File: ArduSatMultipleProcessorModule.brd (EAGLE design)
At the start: 95.5 x 90.3 mm, 86 parts, among them IC1 ATMEGA328P, IC2 ATMEGA328P, IC3 ATMEGA328P, IC4 ATMEGA328P, IC7 ATMEGA328P, IC8 MCP23S17ML, P1 N1_ICSP, P2 N0_ICSP, P3 N0_ICSP, P4 N1_ICSP, P5 N1_ICSP, Q1 BSS138 N-MOSFET, Q10 2N7002 N-MOSFET, Q11 BSS138 N-MOSFET, Q12 BSS138 N-MOSFET, Q2 BSS138 N-MOSFET, Q3 BSS138 N-MOSFET, Q4 BSS138 N-MOSFET, Q5 BSS138 N-MOSFET, Q6 BSS138 N-MOSFET, Q7 BSS138 N-MOSFET, Q8 BSS138 N-MOSFET, Q9 2N7002 N-MOSFET

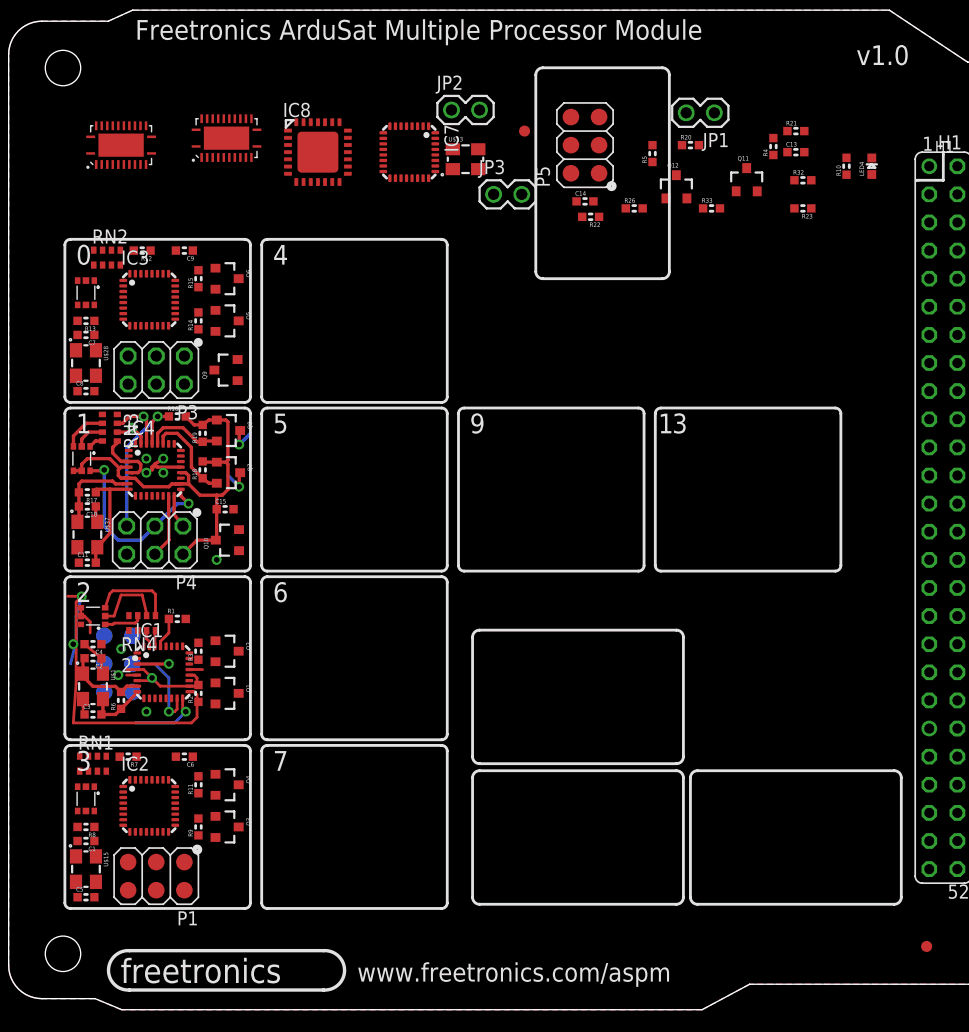
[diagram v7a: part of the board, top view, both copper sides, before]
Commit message: Added parts for remaining nodes
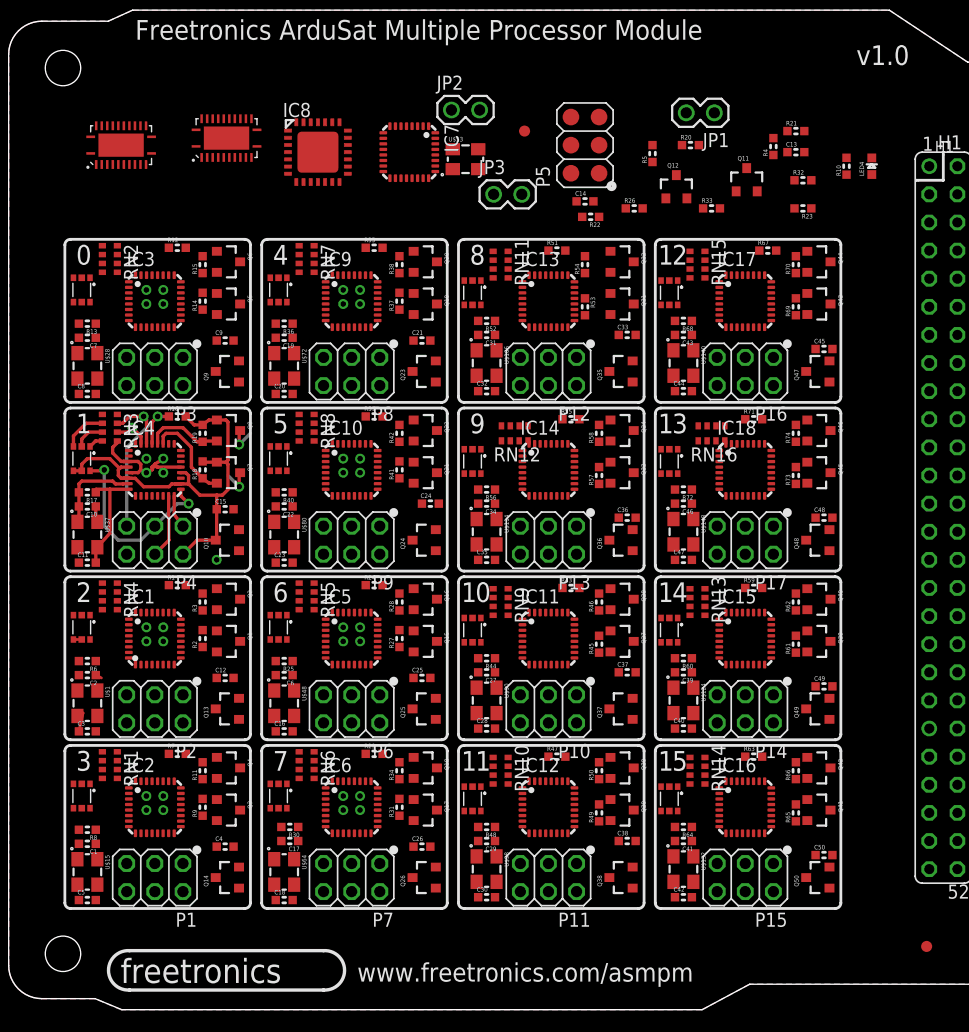
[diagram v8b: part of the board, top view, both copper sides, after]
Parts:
- added C12, C21, C24, C25, C26, C33, C36, C37, C38, C45, C48, C49, C50: 100nF 0603, freetronics-master-v1.1:0603
- added C16, C17, C18, C19, C20, C22, C23, C27, C28, C29, C30, C31, C32, C34, C35, C39, C40, C41, C42, C43, C44, C46, C47: 22pF 0603, freetronics-master-v1.1:0603
- added IC10, IC11, IC12, IC13, IC14, IC15, IC16, IC17, IC18, IC5, IC6, IC9: ATMEGA328P, freetronics-master-v1.1:MLF32
- added P10, P12, P14, P16, P6, P8: N0_ICSP, freetronics-jon:2X03PTH
- added P11, P13, P15, P17, P7, P9: N1_ICSP, freetronics-jon:2X03PTH
- added Q13, Q14, Q23, Q24, Q25, Q26, Q35, Q36, Q37, Q38, Q47, Q48, Q49, Q50: 2N7002 N-MOSFET, freetronics-master-v1:SOT23-3
- added Q15, Q16, Q17, Q18, Q19, Q20, Q21, Q22, Q27, Q28, Q29, Q30, Q31, Q32, Q33, Q34, Q39, Q40, Q41, Q42, Q43, Q44, Q45, Q46: BSS138 N-MOSFET, freetronics-master-v1:SOT23-3
- added R24, R29, R35, R39, R43, R47, R51, R55, R59, R63, R67, R71: 22K 0603, freetronics-master-v1.1:0603
- added R25, R30, R36, R40, R44, R48, R52, R56, R60, R64, R68, R72: 1M 0603, freetronics-master-v1.1:0603
- added R27, R28, R31, R34, R37, R38, R41, R42, R45, R46, R49, R50, R53, R54, R57, R58, R61, R62, R65, R66, R69, R70, R73, R74: 10K 0603, freetronics-master-v1.1:0603
- added RN10, RN11, RN12, RN13, RN14, RN15, RN16, RN5, RN6, RN7, RN8, RN9: 2K2, resistor-dil:CAY16
- added U$106, U$114, U$124, U$132, U$140, U$148, U$48, U$64, U$72, U$80, U$90, U$98: CRYSTAL-GND3X2, freetronics-jon:CRYSTAL-SMD-3X2
- added U$107, U$115, U$125, U$133, U$141, U$149, U$49, U$65, U$73, U$81, U$91, U$99: RGBLEDSMT, freetronics-jon:19-337
- C6: value 100nF 0603 -> 22pF 0603
- P1, P2: device freetronics-jon:2X03SURFACE -> freetronics-jon:2X03PTH
- moved C4 21.8 mm to (19.6, 14.7), turned to 0 degrees
- moved C6 11.6 mm to (24.9, 30.2)
- moved C9 8.92 mm to (19.6, 60.5), turned to 0 degrees
- moved P2 5.24 mm to (13.2, 27.2), flipped to the top, turned to 180 degrees
- moved R2 4.97 mm to (17.5, 33.5)
- moved Q2 4.70 mm to (19.8, 37.1)
- moved Q1 4.70 mm to (19.8, 33.3)
- moved R6 4.68 mm to (7.11, 31.5), turned to 180 degrees
- moved R3 4.46 mm to (17.5, 36.8)
- moved R7 4.45 mm to (15.2, 23.1), turned to 0 degrees
- moved RN4 3.79 mm to (9.14, 37.3), turned to 90 degrees
- moved R12 3.19 mm to (15.2, 68.8), turned to 0 degrees
- moved IC1 3.14 mm to (13.2, 33.5)
- moved R1 3.05 mm to (15.2, 38.4)
- moved R14 1.82 mm to (17.5, 64.0)
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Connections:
- new net N$113: C18.2, IC6.8, R30.1, U$64.3
- new net N$114: C17.2, IC6.7, R30.2, U$64.1
- new net N$115: RN6.6, U$65.3
- new net N$117: RN6.7, U$65.2
- new net N$126: RN6.8, U$65.1
- new net N$182: C20.2, IC9.8, R36.1, U$72.3
- new net N$192: C19.2, IC9.7, R36.2, U$72.1
- new net N$193: C23.2, IC10.8, R40.1, U$80.3
- new net N$194: C22.2, IC10.7, R40.2, U$80.1
- new net N$195: RN8.8, U$81.1
- new net N$196: RN8.6, U$81.3
- new net N$201: RN8.7, U$81.2
- new net N$202: RN7.7, U$73.2
- new net N$214: RN7.6, U$73.3
- new net N$220: RN7.8, U$73.1
- new net N$226: C28.2, IC11.8, R44.1, U$90.3
- new net N$232: C27.2, IC11.7, R44.2, U$90.1
- new net N$233: C30.2, IC12.8, R48.1, U$98.3
- new net N$234: C29.2, IC12.7, R48.2, U$98.1
- new net N$235: C32.2, IC13.8, R52.1, U$106.3
- new net N$24: C16.2, IC5.8, R25.1, U$48.3
- new net N$248: C31.2, IC13.7, R52.2, U$106.1
- new net N$249: C35.2, IC14.8, R56.1, U$114.3
- new net N$250: C34.2, IC14.7, R56.2, U$114.1
- new net N$251: RN12.8, U$115.1
- new net N$252: RN12.6, U$115.3
- new net N$255: RN12.7, U$115.2
- new net N$26: C6.2, IC5.7, R25.2, U$48.1
- new net N$299: RN11.7, U$107.2
- new net N$310: RN11.6, U$107.3
- new net N$311: RN11.8, U$107.1
- new net N$321: C40.2, IC15.8, R60.1, U$124.3
- new net N$338: C39.2, IC15.7, R60.2, U$124.1
- new net N$356: C42.2, IC16.8, R64.1, U$132.3
- new net N$367: C41.2, IC16.7, R64.2, U$132.1
- new net N$374: C44.2, IC17.8, R68.1, U$140.3
- new net N$378: C43.2, IC17.7, R68.2, U$140.1
- new net N$384: C47.2, IC18.8, R72.1, U$148.3
- new net N$39: RN5.6, U$49.3
- new net N$41: RN5.7, U$49.2
- new net N$416: C46.2, IC18.7, R72.2, U$148.1
- new net N$417: RN16.8, U$149.1
- new net N$418: RN16.6, U$149.3
- new net N$419: RN16.7, U$149.2
- new net N$42: RN5.8, U$49.1
- new net N$420: RN15.7, U$141.2
- new net N$421: RN15.6, U$141.3
- new net N$422: RN15.8, U$141.1
- new net N$423: RN9.6, U$91.3
- new net N$424: RN9.7, U$91.2
- new net N$425: RN9.8, U$91.1
- new net N$426: RN10.6, U$99.3
- new net N$427: RN10.7, U$99.2
- new net N$428: RN10.8, U$99.1
- new net N$429: RN13.6, U$125.3
- new net N$430: RN13.7, U$125.2
- new net N$431: RN13.8, U$125.1
- new net N$432: RN14.6, U$133.3
- new net N$433: RN14.7, U$133.2
- new net N$434: RN14.8, U$133.1
- new net N10_5V: C37.1, IC11.18, IC11.20, IC11.4, IC11.6, P10.2, Q27.1, Q28.1, Q37.3, R43.2, R45.2, R46.2, U$91.5, U$91.6
- new net N10_A4_SDA: IC11.27, Q27.2, R45.1
- new net N10_A5_SCL: IC11.28, Q28.2, R46.1
- new net N10_D11_MOSI: IC11.15, P10.4
- new net N10_D12_MISO: IC11.16, P10.1
- new net N10_D13_SCK: IC11.17, P10.3, U$91.4
- new net N10_RESET: IC11.29, P10.5, R43.1
- new net N11_5V: C38.1, IC12.18, IC12.20, IC12.4, IC12.6, P11.2, Q29.1, Q30.1, Q38.3, R47.2, R49.2, R50.2, U$99.5, U$99.6
- new net N11_A4_SDA: IC12.27, Q29.2, R49.1
- new net N11_A5_SCL: IC12.28, Q30.2, R50.1
- new net N11_D11_MOSI: IC12.15, P11.4
- new net N11_D12_MISO: IC12.16, P11.1
- new net N11_D13_SCK: IC12.17, P11.3, U$99.4
- new net N11_RESET: IC12.29, P11.5, R47.1
- new net N12_5V: C45.1, IC17.18, IC17.20, IC17.4, IC17.6, P16.2, Q43.1, Q44.1, Q47.3, R67.2, R69.2, R70.2, U$141.5, U$141.6
- new net N12_A4_SDA: IC17.27, Q43.2, R69.1
- new net N12_A5_SCL: IC17.28, Q44.2, R70.1
- new net N12_D11_MOSI: IC17.15, P16.4
- new net N12_D12_MISO: IC17.16, P16.1
- new net N12_D13_SCK: IC17.17, P16.3, U$141.4
- new net N12_RESET: IC17.29, P16.5, R67.1
- new net N13_5V: C48.1, IC18.18, IC18.20, IC18.4, IC18.6, P17.2, Q45.1, Q46.1, Q48.3, R71.2, R73.2, R74.2, U$149.5, U$149.6
- new net N13_A4_SDA: IC18.27, Q45.2, R73.1
- new net N13_A5_SCL: IC18.28, Q46.2, R74.1
- new net N13_D11_MOSI: IC18.15, P17.4
- new net N13_D12_MISO: IC18.16, P17.1
- new net N13_D13_SCK: IC18.17, P17.3, U$149.4
- new net N13_RESET: IC18.29, P17.5, R71.1
- new net N14_5V: C49.1, IC15.18, IC15.20, IC15.4, IC15.6, P14.2, Q39.1, Q40.1, Q49.3, R59.2, R61.2, R62.2, U$125.5, U$125.6
- new net N14_A4_SDA: IC15.27, Q39.2, R61.1
- new net N14_A5_SCL: IC15.28, Q40.2, R62.1
- new net N14_D11_MOSI: IC15.15, P14.4
- new net N14_D12_MISO: IC15.16, P14.1
- new net N14_D13_SCK: IC15.17, P14.3
- new net N14_RESET: IC15.29, P14.5, R59.1
- new net N15_5V: C50.1, IC16.18, IC16.20, IC16.4, IC16.6, P15.2, Q41.1, Q42.1, Q50.3, R63.2, R65.2, R66.2, U$133.5, U$133.6
- new net N15_A4_SDA: IC16.27, Q41.2, R65.1
- new net N15_A5_SCL: IC16.28, Q42.2, R66.1
- new net N15_D11_MOSI: IC16.15, P15.4
- new net N15_D12_MISO: IC16.16, P15.1
- new net N15_D13_SCK: IC16.17, P15.3, U$133.4
- new net N15_RESET: IC16.29, P15.5, R63.1
- new net N4_5V: C21.1, IC9.18, IC9.20, IC9.4, IC9.6, P8.2, Q19.1, Q20.1, Q23.3, R35.2, R37.2, R38.2, U$73.5, U$73.6
- new net N4_A4_SDA: IC9.27, Q19.2, R37.1
- new net N4_A5_SCL: IC9.28, Q20.2, R38.1
- new net N4_D11_MOSI: IC9.15, P8.4
- new net N4_D12_MISO: IC9.16, P8.1
- new net N4_D13_SCK: IC9.17, P8.3, U$73.4
- new net N4_RESET: IC9.29, P8.5, R35.1
- new net N5_5V: C24.1, IC10.18, IC10.20, IC10.4, IC10.6, P9.2, Q21.1, Q22.1, Q24.3, R39.2, R41.2, R42.2, U$81.5, U$81.6
- new net N5_A4_SDA: IC10.27, Q21.2, R41.1
- new net N5_A5_SCL: IC10.28, Q22.2, R42.1
- new net N5_D11_MOSI: IC10.15, P9.4
- new net N5_D12_MISO: IC10.16, P9.1
- new net N5_D13_SCK: IC10.17, P9.3, U$81.4
- new net N5_RESET: IC10.29, P9.5, R39.1
- new net N6_5V: C25.1, IC5.18, IC5.20, IC5.4, IC5.6, P6.2, Q15.1, Q16.1, Q25.3, R24.2, R27.2, R28.2, U$49.5, U$49.6
- new net N6_A4_SDA: IC5.27, Q15.2, R27.1
- new net N6_A5_SCL: IC5.28, Q16.2, R28.1
- new net N6_D11_MOSI: IC5.15, P6.4
- new net N6_D12_MISO: IC5.16, P6.1
- new net N6_D13_SCK: IC5.17, P6.3, U$125.4, U$49.4
- new net N6_RESET: IC5.29, P6.5, R24.1
- new net N7_5V: C26.1, IC6.18, IC6.20, IC6.4, IC6.6, P7.2, Q17.1, Q18.1, Q26.3, R29.2, R31.2, R34.2, U$65.5, U$65.6
- new net N7_A4_SDA: IC6.27, Q17.2, R31.1
- new net N7_A5_SCL: IC6.28, Q18.2, R34.1
- new net N7_D11_MOSI: IC6.15, P7.4
- new net N7_D12_MISO: IC6.16, P7.1
- new net N7_D13_SCK: IC6.17, P7.3, U$65.4
- new net N7_RESET: IC6.29, P7.5, R29.1
- new net N8_5V: C33.1, IC13.18, IC13.20, IC13.4, IC13.6, P12.2, Q31.1, Q32.1, Q35.3, R51.2, R53.2, R54.2, U$107.5, U$107.6
- new net N8_A4_SDA: IC13.27, Q31.2, R53.1
- new net N8_A5_SCL: IC13.28, Q32.2, R54.1
- new net N8_D11_MOSI: IC13.15, P12.4
- new net N8_D12_MISO: IC13.16, P12.1
- new net N8_D13_SCK: IC13.17, P12.3, U$107.4
- new net N8_RESET: IC13.29, P12.5, R51.1
- new net N9_5V: C36.1, IC14.18, IC14.20, IC14.4, IC14.6, P13.2, Q33.1, Q34.1, Q36.3, R55.2, R57.2, R58.2, U$115.5, U$115.6
- new net N9_A4_SDA: IC14.27, Q33.2, R57.1
- new net N9_A5_SCL: IC14.28, Q34.2, R58.1
- new net N9_D11_MOSI: IC14.15, P13.4
- new net N9_D12_MISO: IC14.16, P13.1
- new net N9_D13_SCK: IC14.17, P13.3, U$115.4
- new net N9_RESET: IC14.29, P13.5, R55.1
- net +5V_SYS: now also Q13.2, Q14.2, Q23.2, Q24.2, Q25.2, Q26.2, Q35.2, Q36.2, Q37.2, Q38.2, Q47.2, Q48.2, Q49.2, Q50.2
- net GND: now also C12.2, C16.1, C17.1, C18.1, C19.1, C20.1, C21.2, C22.1, C23.1, C24.2, C25.2, C26.2, C27.1, C28.1, C29.1, C30.1, C31.1, C32.1, C33.2, C34.1, C35.1, C36.2, C37.2, C38.2, C39.1, C40.1, C41.1, C42.1, C43.1, C44.1, C45.2, C46.1, C47.1, C48.2, C49.2, C50.2, C6.1, IC10.21, IC10.3, IC10.5, IC11.21, IC11.3, IC11.5, IC12.21, IC12.3, IC12.5, IC13.21, IC13.3, IC13.5, IC14.21, IC14.3, IC14.5, IC15.21, IC15.3, IC15.5, IC16.21, IC16.3, IC16.5, IC17.21, IC17.3, IC17.5, IC18.21, IC18.3, IC18.5, IC5.21, IC5.3, IC5.5, IC6.21, IC6.3, IC6.5, IC9.21, IC9.3, IC9.5, P10.6, P11.6, P12.6, P13.6, P14.6, P15.6, P16.6, P17.6, P6.6, P7.6, P8.6, P9.6, RN1.1, RN10.1, RN11.1, RN12.1, RN13.1, RN14.1, RN15.1, RN16.1, RN2.1, RN4.1, RN5.1, RN6.1, RN7.1, RN8.1, RN9.1, U$106.2, U$106.4, U$114.2, U$114.4, U$124.2, U$124.4, U$132.2, U$132.4, U$140.2, U$140.4, U$148.2, U$148.4, U$48.2, U$48.4, U$64.2, U$64.4, U$72.2, U$72.4, U$80.2, U$80.4, U$90.2, U$90.4, U$98.2, U$98.4; no longer C6.2, RN1.2, RN2.2, RN4.2
- net N$10: now also RN1.8; no longer RN1.7
- net N$13: now also RN2.7; no longer RN2.6
- net N$15: now also RN2.6; no longer RN2.5
- net N$16: now also RN2.8; no longer RN2.7
- net N$4: now also U$9.3; no longer U$9.2
- net N$5: now also RN4.7, U$9.2; no longer RN4.5, U$9.3
- net N$6: now also RN4.8; no longer RN4.7
- net N$8: now also U$16.3; no longer U$16.2
- net N$9: now also RN1.7, U$16.2; no longer RN1.5, U$16.3
- net N0_D0_RX: now also RN2.3; no longer RN2.4
- net N0_D1_TX: now also RN2.2; no longer RN2.3
- net N10_D0_RX: now also IC11.30, RN9.3
- net N10_D1_TX: now also IC11.31, RN9.2
- net N10_PWR: now also Q37.1
- net N11_D0_RX: now also IC12.30, RN10.3
- net N11_D1_TX: now also IC12.31, RN10.2
- net N11_PWR: now also Q38.1
- net N12_D0_RX: now also IC17.30, RN15.3
- net N12_D1_TX: now also IC17.31, RN15.2
- net N12_PWR: now also Q47.1
- net N13_D0_RX: now also IC18.30, RN16.3
- net N13_D1_TX: now also IC18.31, RN16.2
- net N13_PWR: now also Q48.1
- net N14_D0_RX: now also IC15.30, RN13.3
- net N14_D1_TX: now also IC15.31, RN13.2
- net N14_PWR: now also Q49.1
- net N15_D0_RX: now also IC16.30, RN14.3
- net N15_D1_TX: now also IC16.31, RN14.2
- net N15_PWR: now also Q50.1
- net N2_5V: now also C12.1, Q13.3; no longer C4.1
- net N2_D0_RX: now also RN4.3; no longer RN4.4
- net N2_D1_TX: now also RN4.2; no longer RN4.3
- net N2_PWR: now also Q13.1
- net N3_5V: now also C4.1, Q14.3; no longer C6.1
- net N3_D0_RX: now also RN1.3; no longer RN1.4
- net N3_D1_TX: now also RN1.2; no longer RN1.3
- net N3_PWR: now also Q14.1
- net N4_D0_RX: now also IC9.30, RN7.3
- net N4_D1_TX: now also IC9.31, RN7.2
- net N4_PWR: now also Q23.1
- net N5_D0_RX: now also IC10.30, RN8.3
- net N5_D1_TX: now also IC10.31, RN8.2
- net N5_PWR: now also Q24.1
- net N6_D0_RX: now also IC5.30, RN5.3
- net N6_D1_TX: now also IC5.31, RN5.2
- net N6_PWR: now also Q25.1
- net N7_D0_RX: now also IC6.30, RN6.3
- net N7_D1_TX: now also IC6.31, RN6.2
- net N7_PWR: now also Q26.1
- net N8_D0_RX: now also IC13.30, RN11.3
- net N8_D1_TX: now also IC13.31, RN11.2
- net N8_PWR: now also Q35.1
- net N9_D0_RX: now also IC14.30, RN12.3
- net N9_D1_TX: now also IC14.31, RN12.2
- net N9_PWR: now also Q36.1
- net NODE_SCL: now also Q16.3, Q18.3, Q20.3, Q22.3, Q28.3, Q30.3, Q32.3, Q34.3, Q40.3, Q42.3, Q44.3, Q46.3
- net NODE_SDA: now also Q15.3, Q17.3, Q19.3, Q21.3, Q27.3, Q29.3, Q31.3, Q33.3, Q39.3, Q41.3, Q43.3, Q45.3
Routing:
- net N2_D13_SCK: track 33.4 -> 0.00 mm, vias 1 -> 0
- net N2_5V: track 12.6 -> 0.75 mm, vias 1 -> 0
- net N$5: track 7.64 -> 0.00 mm
- net N$2: track 7.48 -> 0.00 mm
- net GND: track 22.9 -> 15.5 mm, vias 10 -> 33
- net N2_D11_MOSI: track 6.65 -> 0.00 mm, vias 1 -> 0
- net N$4: track 6.63 -> 0.00 mm
- net N2_D12_MISO: track 6.33 -> 0.00 mm, vias 1 -> 0
- net N$7: track 5.54 -> 0.00 mm
- net N$6: track 3.53 -> 0.00 mm
- net N2_RESET: track 2.79 -> 0.00 mm
- net N2_D1_TX: track 1.51 -> 0.00 mm
- net N2_D0_RX: track 1.38 -> 0.00 mm
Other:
- board text added: "8"
- board text added: "www.freetronics.com/asmpm"
- board text removed: "www.freetronics.com/aspm"
